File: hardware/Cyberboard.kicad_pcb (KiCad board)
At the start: 4 copper layers, 51 x 21 mm, 69 parts, among them J1 Conn_01x20, J2 Conn_01x20, SW1 SW_Push, SW2 SW_Push, U1 SZYY0402Y_C434450, U10 XL-1005UBC_C22355736, U2 TPD2EUSB30, U3 NX2012SA-32.768KHZ-STD-MUB-2, U4 STM32WB55RGVx, U5 BQ24072RGT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

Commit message: started PCB
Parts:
- moved R12 48.8 mm to (215.2, 99.1)
- moved C20 47.7 mm to (213.4, 96.6), turned to 180 degrees
- moved R11 46.1 mm to (212.9, 98.6), turned to 180 degrees
- moved C23 45.2 mm to (215.4, 95.6)
- moved U8 40.7 mm to (215.4, 97.2)
- moved U5 39.3 mm to (160.0, 76.7), turned to 180 degrees
- moved U9 34.9 mm to (141.1, 108.0)
- moved U6 33.6 mm to (141.1, 105.4)
- moved R10 32.7 mm to (140.5, 103.8), turned to 180 degrees
- moved R9 32.6 mm to (139.4, 105.5), turned to -90 degrees
- moved C24 32.5 mm to (199.2, 122.1), turned to 90 degrees
- moved C27 32.5 mm to (200.2, 122.1), turned to 90 degrees
- moved C22 31.8 mm to (137.8, 105.0), turned to 90 degrees
- moved C19 31.7 mm to (196.5, 123.9)
- moved C21 22.4 mm to (143.0, 104.6), turned to 90 degrees
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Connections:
- C7 pad 1: Net-(C7-Pad1) -> Net-(U4-VFBSMPS)
- L1 pad 2: Net-(C7-Pad1) -> Net-(U4-VFBSMPS)
- U4 pad 10: /GPIO1 -> /GPIO0
- U4 pad 11: /GPIO2 -> /GPIO1
- U4 pad 12: /GPIO3 -> /GPIO2
- U4 pad 15: /GPIO4 -> /GPIO3
- U4 pad 16: /GPIO5 -> /GPIO4
- U4 pad 17: /GPIO6 -> /GPIO5
- U4 pad 18: /GPIO7 -> /GPIO6
- U4 pad 19: /GPIO8 -> /GPIO7
- U4 pad 2: unconnected-(U4-PC13-Pad2) -> /ICM_CS
- U4 pad 20: /GPIO9 -> /GPIO8
- U4 pad 21: /GPIO10 -> /GPIO9
- U4 pad 22: /GPIO11 -> /GPIO10
- U4 pad 23: /GPIO12 -> /GPIO11
- U4 pad 24: /GPIO13 -> /GPIO12
- U4 pad 25: /GPIO14 -> /GPIO13
- U4 pad 26: /GPIO15 -> /GPIO14
- U4 pad 27: unconnected-(U4-PB2-Pad27) -> /GPIO15
- U4 pad 38: unconnected-(U4-PB0-Pad38) -> /GPIO16
- U4 pad 39: unconnected-(U4-PB1-Pad39) -> /GPIO17
- U4 pad 40: unconnected-(U4-PE4-Pad40) -> /GPIO18
- U4 pad 41: unconnected-(U4-VFBSMPS-Pad41) -> Net-(U4-VFBSMPS)
- U4 pad 46: /GPIO16 -> /GPIO19
- U4 pad 47: /GPIO17 -> /GPIO20
- U4 pad 48: /GPIO18 -> /GPIO21
- U4 pad 49: /GPIO19 -> /GPIO22
- U4 pad 50: /GPIO20 -> /GPIO23
- U4 pad 51: /GPIO21 -> /GPIO24
- U4 pad 57: /GPIO22 -> /GPIO25
- U4 pad 58: /GPIO23 -> /GPIO26
- U4 pad 59: /GPIO24 -> /GPIO27
- U4 pad 6: unconnected-(U4-PB8-Pad6) -> /BMP_SCL
- U4 pad 60: /GPIO25 -> /GPIO28
- U4 pad 61: /GPIO26 -> /GPIO29
- U4 pad 62: /GPIO27 -> /LED
- U4 pad 63: /GPIO28 -> /ICM_SCK
- U4 pad 64: /GPIO29 -> /ICM_MISO
- U4 pad 65: /LED -> /ICM_MOSI
- U4 pad 66: unconnected-(U4-PB6-Pad66) -> /ICM_INT1
- U4 pad 67: unconnected-(U4-PB7-Pad67) -> /ICM_INT2
- U4 pad 7: unconnected-(U4-PB9-Pad7) -> /BMP_SDA
- U4 pad 9: /GPIO0 -> /BMP_INT
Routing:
- net VCC: vias 2 -> 0
- net VBUS: vias 2 -> 0
- net Net-(C26-Pad1): vias 1 -> 0
- net GND: vias 87 -> 59
- net /SWDIO: vias 1 -> 0
- net /SWCLK: vias 1 -> 0
- net /GPIO7: vias 1 -> 0
- net /GPIO6: vias 1 -> 0
- net /GPIO5: vias 1 -> 0
- net /GPIO4: vias 1 -> 0
- net /GPIO3: vias 1 -> 0
- net /GPIO29: vias 1 -> 0
- net /GPIO28: vias 1 -> 0
- net /GPIO27: vias 1 -> 0
- net /GPIO26: vias 1 -> 0
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
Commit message: start routing
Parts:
- removed D1: PESD15VL1BA, Diode_SMD:D_SOD-323
- C14, C17: footprint Capacitor_SMD:C_0603_1608Metric -> Capacitor_SMD:C_0402_1005Metric
- C25, C26: footprint Capacitor_SMD:C_0402_1005Metric -> Capacitor_SMD:C_0603_1608Metric
- moved C27 67.6 mm to (147.8, 79.5), turned to 0 degrees
- moved R12 67.5 mm to (149.7, 82.4), turned to 180 degrees
- moved C24 66.2 mm to (147.8, 80.5), turned to 0 degrees
- moved U8 65.2 mm to (151.8, 83.0), turned to -90 degrees
- moved U7 64.5 mm to (145.6, 82.3), turned to 90 degrees
- moved R11 64.3 mm to (151.0, 81.3)
- moved C19 64.2 mm to (147.8, 82.1), turned to 90 degrees
- moved C23 63.3 mm to (153.4, 82.9), turned to -90 degrees
- moved C20 62.9 mm to (152.5, 80.8), turned to 90 degrees
- moved L2 49.4 mm to (131.9, 82.4), turned to -90 degrees
- moved L1 49.3 mm to (130.4, 81.2), turned to -90 degrees
- moved C17 47.6 mm to (141.0, 71.4)
- moved C14 45.8 mm to (130.1, 78.7), turned to -90 degrees
- moved C13 44.8 mm to (131.1, 78.7), turned to -90 degrees
- moved C5 44.2 mm to (133.1, 73.6), turned to 90 degrees
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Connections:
- R11 pad 1: /I2C_SCL -> /BMP_SCL
- R12 pad 1: /I2C_SDA -> /BMP_SDA
- U4 pad 2: /ICM_CS -> /LED
- U4 pad 38: /GPIO16 -> /GPIO18
- U4 pad 40: /GPIO18 -> /GPIO16
- U4 pad 58: /GPIO26 -> /GPIO28
- U4 pad 59: /GPIO27 -> /GPIO29
- U4 pad 60: /GPIO28 -> /GPIO27
- U4 pad 61: /GPIO29 -> /GPIO26
- U4 pad 62: /LED -> /ICM_CS
- U7 pad 4: /ICM_INT2 -> /ICM_INT1
- U8 pad 2: /I2C_SCL -> /BMP_SCL
- U8 pad 4: /I2C_SDA -> /BMP_SDA
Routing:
- net +3.3V: track 0.00 -> 50.2 mm, vias 0 -> 18
- net /DN: track 0.00 -> 35.5 mm
- net /DP: track 0.00 -> 35.3 mm
- net /GPIO0: track 0.00 -> 32.8 mm, vias 0 -> 1
- net /GPIO1: track 0.00 -> 30.4 mm, vias 0 -> 1
- net /GPIO29: track 0.00 -> 30.3 mm, vias 0 -> 1
- net VBUS: track 0.00 -> 29.6 mm, vias 0 -> 2
- net /BOOT: track 0.00 -> 27.2 mm, vias 0 -> 2
- net GND: track 0.00 -> 26.0 mm, vias 59 -> 60
- net /GPIO2: track 0.00 -> 25.5 mm, vias 0 -> 1
- net /GPIO28: track 0.00 -> 25.5 mm, vias 0 -> 1
- net /RESET: track 0.00 -> 24.5 mm, vias 0 -> 2
- net /GPIO3: track 0.00 -> 23.8 mm, vias 0 -> 1
- net VCC: track 0.00 -> 23.8 mm, vias 0 -> 2
- net /GPIO4: track 0.00 -> 21.7 mm, vias 0 -> 1
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- added copper zone on F.Cu, net +3.3V

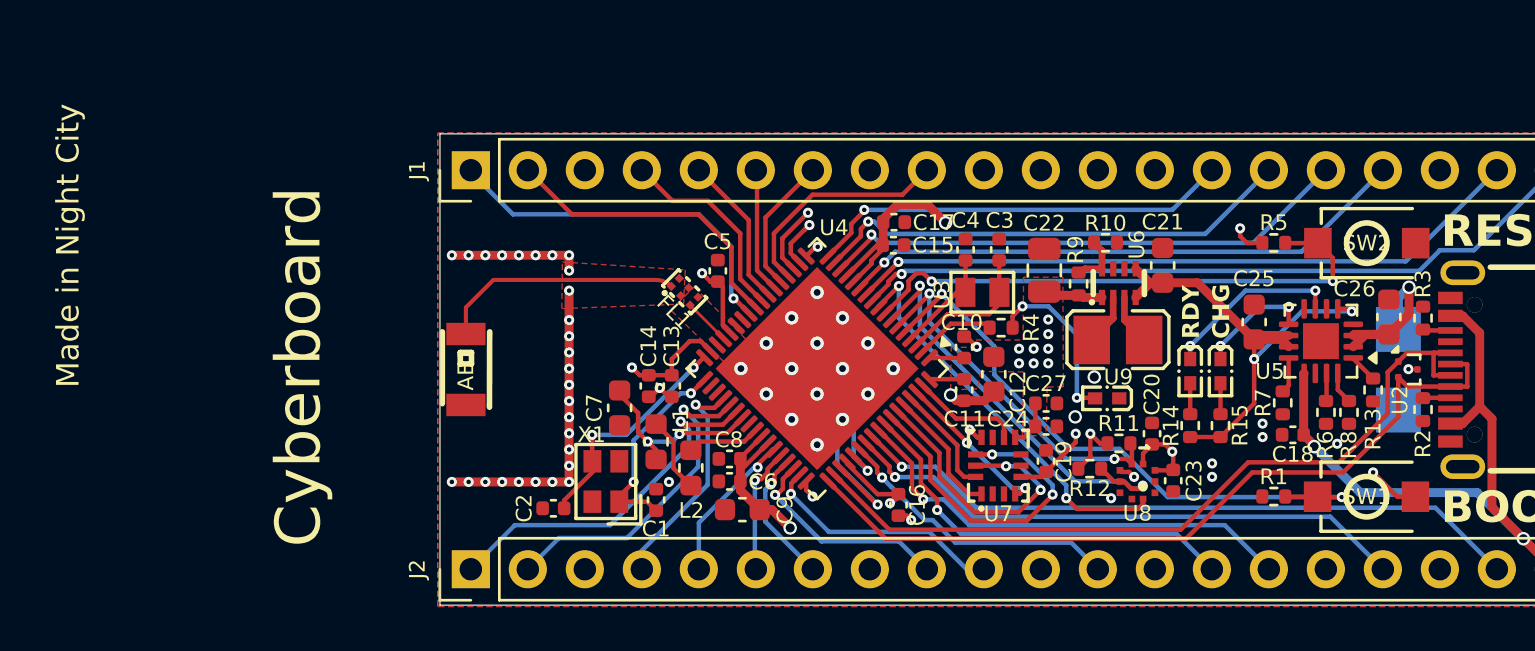
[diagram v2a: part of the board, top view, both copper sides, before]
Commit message: finish routing and antenna
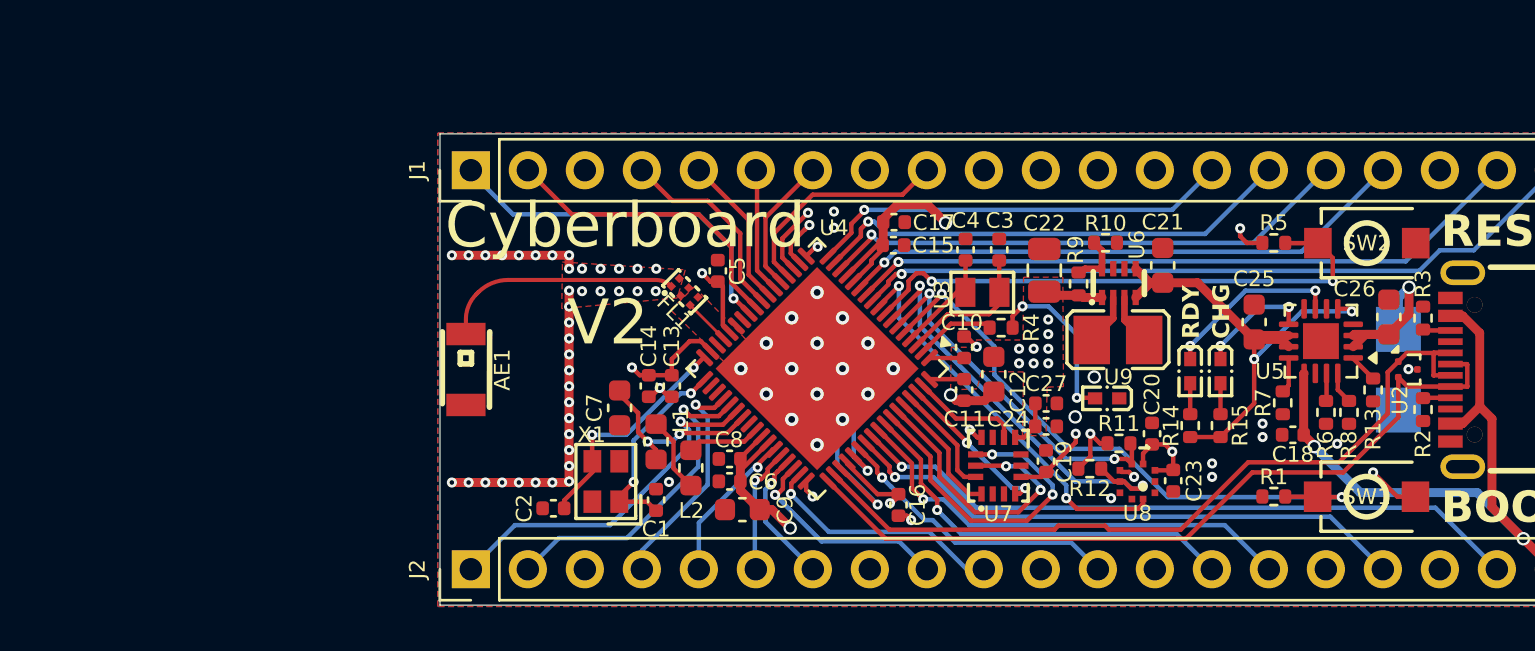
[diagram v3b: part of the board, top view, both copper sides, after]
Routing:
- net GND: track 26.0 -> 25.9 mm, vias 60 -> 73
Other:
- board text added: "V2"
- board text removed: "Made in Night City"

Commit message: add stuff
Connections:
- U4 pad 38: /GPIO18 -> /GPIO16
- U4 pad 40: /GPIO16 -> /GPIO18
- U4 pad 58: /GPIO28 -> /GPIO26
- U4 pad 59: /GPIO29 -> /GPIO27
- U4 pad 60: /GPIO27 -> /GPIO28
- U4 pad 61: /GPIO26 -> /GPIO29
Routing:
- net /GPIO18: track 10.3 -> 12.0 mm
- net /GPIO17: track 14.7 -> 13.5 mm
- net /GPIO16: track 16.0 -> 16.6 mm
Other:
- board text added: "EXE"
- board text added: "Made in Night City"

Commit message: rounded corners and new renders and flyer
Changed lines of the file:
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@@
+	)
+	(segment
+		(start 165.77 77.25)
+		(end 165.02 77.25)
+		(width 0.2)
+		(layer "F.Cu")
+		(net 27)
 	)
 	(segment
@@
 	)
 	(segment
+		(start 165.019 77.251)
+		(end 165.019 78.094)
+		(width 0.2)
+		(layer "F.Cu")
+		(net 27)
+	)
+	(segment
+		(start 165.019 78.094)
+		(end 165.175 78.25)
+		(width 0.2)
+		(layer "F.Cu")
+		(net 27)
+	)
+	(segment
 		(start 156.756802 82.125)
 		(end 160.806802 82.125)
@@
 	)
 	(segment
-		(start 165.77 77.25)
-		(end 165.02 77.25)
-		(width 0.2)
-		(layer "F.Cu")
-		(net 27)
-	)
-	(segment
-		(start 165.019 78.249)
-		(end 165.02 78.25)
+		(start 165.175 78.25)
+		(end 165.77 78.25)
 		(width 0.2)
 		(layer "F.Cu")
@@
 	)
 	(segment
-		(start 165.02 78.25)
-		(end 165.77 78.25)
-		(width 0.2)
-		(layer "F.Cu")
-		(net 27)
-	)
-	(segment
-		(start 165.019 77.251)
-		(end 165.019 78.249)
-		(width 0.2)
-		(layer "F.Cu")
-		(net 27)
-	)
-	(segment
 		(start 150.375 84.95)
 		(end 150.55 85.125)
@@
 	)
 	(segment
-		(start 166.521 78.749)
-		(end 166.52 78.75)
-		(width 0.2)
-		(layer "F.Cu")
-		(net 28)
-	)
-	(segment
-		(start 165.77 77.75)
-		(end 166.5 77.75)
+		(start 166.521 77.921)
+		(end 166.521 78.579)
+		(width 0.2)
+		(layer "F.Cu")
+		(net 28)
+	)
+	(segment
+		(start 166.35 77.75)
+		(end 166.521 77.921)
 		(width 0.2)
 		(layer "F.Cu")
@@
 	)
 	(segment
+		(start 165.77 77.75)
+		(end 166.35 77.75)
+		(width 0.2)
+		(layer "F.Cu")
+		(net 28)
+	)
+	(segment
 		(start 165.77 78.75)
 		(end 163.86 78.75)
@@
 	)
 	(segment
+		(start 166.35 78.75)
+		(end 165.77 78.75)
+		(width 0.2)
+		(layer "F.Cu")
+		(net 28)
+	)
+	(segment
 		(start 160.993198 82.575)
 		(end 156.943198 82.575)
@@
 	)
 	(segment
-		(start 166.521 77.771)
-		(end 166.521 78.749)
-		(width 0.2)
-		(layer "F.Cu")
-		(net 28)
-	)
-	(segment
 		(start 140.599517 85.525)
 		(end 138.036136 82.961619)
@@
 	)
 	(segment
-		(start 166.52 78.75)
-		(end 165.77 78.75)
-		(width 0.2)
-		(layer "F.Cu")
-		(net 28)
-	)
-	(segment
-		(start 166.5 77.75)
-		(end 166.521 77.771)
-		(width 0.2)
-		(layer "F.Cu")
-		(net 28)
-	)
-	(segment
 		(start 163.4475 78.3375)
 		(end 163.4475 80.120698)
@@
 		(width 0.2)
 		(layer "F.Cu")
+		(net 28)
+	)
+	(segment
+		(start 166.521 78.579)
+		(end 166.35 78.75)
+		(width 0.2)
+		(layer "F.Cu")

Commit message: final final bluetooth trace udpate
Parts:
- added R16: 4.7K, Resistor_SMD:R_0402_1005Metric, F.Cu at (149.7, 83.5)
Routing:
- net GND: track 25.9 -> 33.2 mm, vias 73 -> 85
- net /ICM_CS: track 14.6 -> 16.1 mm
- net +3.3V: track 50.2 -> 50.7 mm, vias 18 -> 19
